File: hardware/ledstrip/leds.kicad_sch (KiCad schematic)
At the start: 4 parts, among them J5 Ledstrip connector, Q1 Q_NMOS, Q2 Q_NMOS, Q3 Q_NMOS

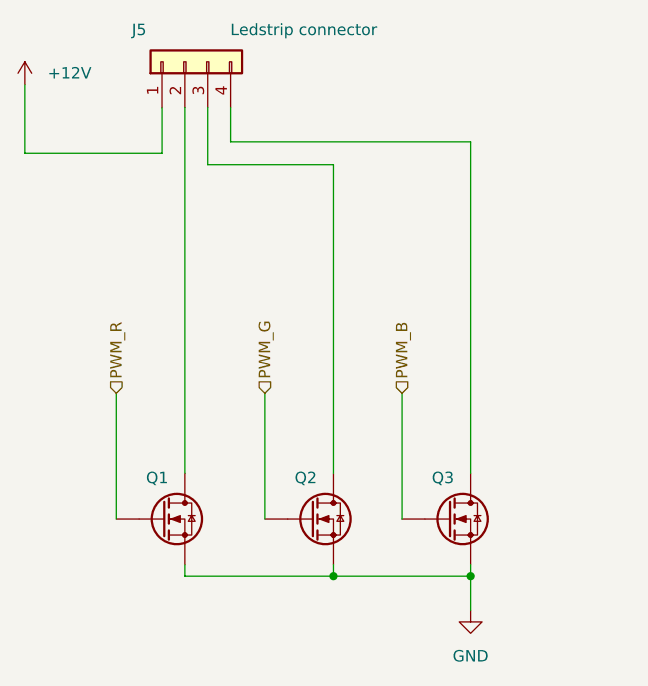
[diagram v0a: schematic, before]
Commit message: Add label on nodes.
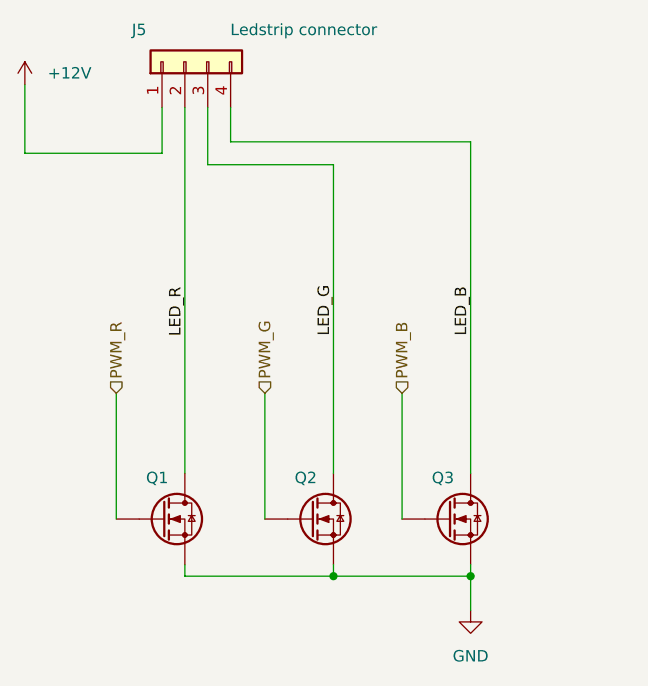
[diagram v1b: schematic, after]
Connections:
- net LED_G: now reaches J5.3 (Pin_3), Q2.D
- net LED_R: now reaches J5.2 (Pin_2), Q1.D
- net LED_B: now reaches J5.4 (Pin_4), Q3.D
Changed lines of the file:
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@@
+		)
+	)
+	(label "LED_R"
+		(at 116.84 88.9 90)
+		(effects
+			(font
+				(size 1.27 1.27)
+			)
+			(justify left bottom)
+		)
+	)
+	(label "LED_B"
+		(at 148.59 88.8363 90)
+		(effects
+			(font
+				(size 1.27 1.27)
+			)
+			(justify left bottom)
+		)
+	)
+	(label "LED_G"
+		(at 133.35 88.8363 90)
+		(effects
+			(font
+				(size 1.27 1.27)
+			)
+			(justify left bottom)
 		)
 	)

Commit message: Continue PCB.
Create netlists and color them.
Fix wrong symbol pin <-> foot print pins mapping.
Replace footprint and part for leds N-MOSFET.
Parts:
- Q1, Q2, Q3: footprint Package_TO_SOT_SMD:SOT-23_Handsoldering -> TOT-220-3:TO-220-3_Vertical; Distributor Link 1 https://www.amazon.fr/Aexit-canaux-AO3400A-Transistor-BM621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 -> https://www.mouser.fr/ProductDetail/Infineon-Technologies/I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; Distributor Link 2 https://www.digikey.fr/fr/products/detail/alpha-omega-semic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 -> https://www.digikey.fr/fr/products/detail/infineon-technolo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
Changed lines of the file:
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@@
+	(symbol
+		(lib_id "Device:Q_NMOS")
+		(at 146.05 109.22 0)
+		(unit 1)
+		(exclude_from_sim no)
+		(in_bom yes)
+		(on_board yes)
+		(dnp no)
+		(property "Reference" "Q3"
+			(at 144.272 104.648 0)
+			(effects
+				(font
+					(size 1.27 1.27)
+				)
+				(justify left)
+			)
+		)
+		(property "Value" "Q_NMOS"
+			(at 149.606 104.648 0)
+			(effects
+				(font
+					(size 1.27 1.27)
+				)
+				(justify left)
+				(hide yes)
+			)
+		)
+		(property "Footprint" "TOT-220-3:TO-220-3_Vertical"
+			(at 151.13 106.68 0)
+			(effects
+				(font
+					(size 1.27 1.27)
+				)
+				(hide yes)
+			)
+		)
+		(property "Datasheet" "https://www.mouser.fr/datasheet/3/70/1/Infineon-IRL3705N-DS-v01_02-EN.pdf"
+			(at 146.05 109.22 0)
+			(effects
+				(font
+					(size 1.27 1.27)
+				)
+				(hide yes)
+			)
+		)
+		(property "Description" "N-MOSFET transistor"
+			(at 146.05 109.22 0)
+			(effects
+				(font
+					(size 1.27 1.27)
+				)
+				(hide yes)
+			)
+		)
+		(property "Distributor Link 1" "https://www.mouser.fr/ProductDetail/Infineon-Technologies/IRL3705NPBF?qs=9%252BKlkBgLFf3RbtP30EBJKw%3D%3D"
+			(at 146.05 109.22 0)
+			(effects
+				(font
+					(size 1.27 1.27)
+				)
+				(hide yes)
+			)
+		)
+		(property "Distributor Link 2" "https://www.digikey.fr/fr/products/detail/infineon-technologies/IRL3705NPBF/812272?srsltid=AfmBOoooeDWkDS-ehnbFZ027sJbqecXx9GdmwNsCp8G_IMCaE9HrNfFl"
+			(at 146.05 109.22 0)
+			(effects
+				(font
+					(size 1.27 1.27)
+				)
+				(hide yes)
+			)
+		)
+		(pin "S"
+		)
+		(pin "D"
+		)
+		(pin "G"
+		)
+		(instances
+			(project "ledstrip"
+				(path "/dcb997ee-94c4-4df2-ba22-0e091735ddd7/ee2150f8-5f25-45fa-a64e-caf3b7331721"
+					(reference "Q3")
+					(unit 1)
+				)
+			)
+		)
+	)
+	(symbol
+		(lib_id "Device:Q_NMOS")
+		(at 114.3 109.22 0)
+		(unit 1)
+		(exclude_from_sim no)
+		(in_bom yes)
+		(on_board yes)
+		(dnp no)
+		(property "Reference" "Q1"
+			(at 112.522 104.648 0)
+			(effects
+				(font
+					(size 1.27 1.27)
+				)
+				(justify left)
+			)
+		)
+		(property "Value" "Q_NMOS"
+			(at 117.856 104.648 0)
+			(effects
+				(font
+					(size 1.27 1.27)
+				)
+				(justify left)
+				(hide yes)
+			)
+		)
+		(property "Footprint" "TOT-220-3:TO-220-3_Vertical"
+			(at 119.38 106.68 0)
+			(effects
+				(font
+					(size 1.27 1.27)
+				)
+				(hide yes)
+			)
+		)
+		(property "Datasheet" "https://www.mouser.fr/datasheet/3/70/1/Infineon-IRL3705N-DS-v01_02-EN.pdf"
+			(at 114.3 109.22 0)
+			(effects
+				(font
+					(size 1.27 1.27)
+				)
+				(hide yes)
+			)
+		)
+		(property "Description" "N-MOSFET transistor"
+			(at 114.3 109.22 0)
+			(effects
+				(font
+					(size 1.27 1.27)
+				)
+				(hide yes)
+			)
+		)
+		(property "Distributor Link 1" "https://www.mouser.fr/ProductDetail/Infineon-Technologies/IRL3705NPBF?qs=9%252BKlkBgLFf3RbtP30EBJKw%3D%3D"
+			(at 114.3 109.22 0)
+			(effects
+				(font
+					(size 1.27 1.27)
+				)
+				(hide yes)
+			)
+		)
+		(property "Distributor Link 2" "https://www.digikey.fr/fr/products/detail/infineon-technologies/IRL3705NPBF/812272?srsltid=AfmBOoooeDWkDS-ehnbFZ027sJbqecXx9GdmwNsCp8G_IMCaE9HrNfFl"
+			(at 114.3 109.22 0)
+			(effects
+				(font
+					(size 1.27 1.27)
+				)
+				(hide yes)
+			)
+		)
+		(pin "S"
+		)
+		(pin "D"
+		)
+		(pin "G"
+		)
+		(instances
+			(project ""
+				(path "/dcb997ee-94c4-4df2-ba22-0e091735ddd7/0b9dc6db-254f-4d56-b53f-9075578fa80e"
+					(reference "Q1")
+					(unit 1)
+				)
+				(path "/dcb997ee-94c4-4df2-ba22-0e091735ddd7/ee2150f8-5f25-45fa-a64e-caf3b7331721"
+					(reference "Q1")
+					(unit 1)
+				)
+			)
+		)
+	)
 	(symbol
 		(lib_id "Device:Q_NMOS")
@@
 			)
 		)
-		(property "Footprint" "Package_TO_SOT_SMD:SOT-23_Handsoldering"
+		(property "Footprint" "TOT-220-3:TO-220-3_Vertical"
 			(at 135.89 106.68 0)
 			(effects
@@
 			)
 		)
-		(property "Datasheet" "https://mm.digikey.com/Volume0/opasdata/https://mm.digikey.com/Volume0/opasdata/d220001/medias/docus/1133/AO3400A_ds.pdf/medias/docus/1133/AO3400A_ds.pdf"
+		(property "Datasheet" "https://www.mouser.fr/datasheet/3/70/1/Infineon-IRL3705N-DS-v01_02-EN.pdf"
 			(at 130.81 109.22 0)
 			(effects
@@
 			)
 		)
-		(property "Distributor Link 1" "https://www.amazon.fr/Aexit-canaux-AO3400A-Transistor-BM621825K482219I/dp/B07DD8V1JR"
+		(property "Distributor Link 1" "https://www.mouser.fr/ProductDetail/Infineon-Technologies/IRL3705NPBF?qs=9%252BKlkBgLFf3RbtP30EBJKw%3D%3D"
 			(at 130.81 109.22 0)
 			(effects
@@
 			)
 		)
-		(property "Distributor Link 2" "https://www.digikey.fr/fr/products/detail/alpha-omega-semiconductor-inc/AO3400A/1855772?srsltid=AfmBOorsNVseuGnOsg8gC49lTDXI5zjjIDAef0vv8GR8XI0_NYzzrFG-"
+		(property "Distributor Link 2" "https://www.digikey.fr/fr/products/detail/infineon-technologies/IRL3705NPBF/812272?srsltid=AfmBOoooeDWkDS-ehnbFZ027sJbqecXx9GdmwNsCp8G_IMCaE9HrNfFl"
 			(at 130.81 109.22 0)
 			(effects
@@
 				(path "/dcb997ee-94c4-4df2-ba22-0e091735ddd7/ee2150f8-5f25-45fa-a64e-caf3b7331721"
 					(reference "Q2")
-					(unit 1)
-				)
-			)
-		)
-	)
-	(symbol
-		(lib_id "Device:Q_NMOS")
-		(at 114.3 109.22 0)
-		(unit 1)
-		(exclude_from_sim no)
-		(in_bom yes)
-		(on_board yes)
-		(dnp no)
-		(property "Reference" "Q1"
-			(at 112.522 104.648 0)
-			(effects
-				(font
-					(size 1.27 1.27)
-				)
-				(justify left)
-			)
-		)
-		(property "Value" "Q_NMOS"
-			(at 117.856 104.648 0)
-			(effects
-				(font
-					(size 1.27 1.27)
-				)
-				(justify left)
-				(hide yes)
-			)
-		)
-		(property "Footprint" "Package_TO_SOT_SMD:SOT-23_Handsoldering"
-			(at 119.38 106.68 0)
-			(effects
-				(font
-					(size 1.27 1.27)
-				)
-				(hide yes)
-			)
-		)
-		(property "Datasheet" "https://mm.digikey.com/Volume0/opasdata/https://mm.digikey.com/Volume0/opasdata/d220001/medias/docus/1133/AO3400A_ds.pdf/medias/docus/1133/AO3400A_ds.pdf"
-			(at 114.3 109.22 0)
-			(effects
-				(font
-					(size 1.27 1.27)
-				)
-				(hide yes)
-			)
-		)
-		(property "Description" "N-MOSFET transistor"
-			(at 114.3 109.22 0)
-			(effects
-				(font
-					(size 1.27 1.27)
-				)
-				(hide yes)
-			)
-		)
-		(property "Distributor Link 1" "https://www.amazon.fr/Aexit-canaux-AO3400A-Transistor-BM621825K482219I/dp/B07DD8V1JR"
-			(at 114.3 109.22 0)
-			(effects
-				(font
-					(size 1.27 1.27)
-				)
-				(hide yes)
-			)
-		)
-		(property "Distributor Link 2" "https://www.digikey.fr/fr/products/detail/alpha-omega-semiconductor-inc/AO3400A/1855772?srsltid=AfmBOorsNVseuGnOsg8gC49lTDXI5zjjIDAef0vv8GR8XI0_NYzzrFG-"
-			(at 114.3 109.22 0)
-			(effects
-				(font
-					(size 1.27 1.27)
-				)
-				(hide yes)
-			)
-		)
-		(pin "S"
-		)
-		(pin "D"
-		)
-		(pin "G"
-		)
-		(instances
-			(project "ledstrip"
-				(path "/dcb997ee-94c4-4df2-ba22-0e091735ddd7/ee2150f8-5f25-45fa-a64e-caf3b7331721"
-					(reference "Q1")
 					(unit 1)
 				)
@@
 					(unit 1)
 				)
-			)
-		)
-	)
-	(symbol
-		(lib_id "Device:Q_NMOS")
-		(at 146.05 109.22 0)
-		(unit 1)
-		(exclude_from_sim no)
-		(in_bom yes)
-		(on_board yes)
-		(dnp no)
-		(property "Reference" "Q3"
-			(at 144.272 104.648 0)
-			(effects
-				(font
-					(size 1.27 1.27)
-				)
-				(justify left)
-			)
-		)
-		(property "Value" "Q_NMOS"
-			(at 149.606 104.648 0)
-			(effects
-				(font
-					(size 1.27 1.27)
-				)
-				(justify left)
-				(hide yes)
-			)
-		)
-		(property "Footprint" "Package_TO_SOT_SMD:SOT-23_Handsoldering"
-			(at 151.13 106.68 0)
-			(effects
-				(font
-					(size 1.27 1.27)
-				)
-				(hide yes)
-			)
-		)
-		(property "Datasheet" "https://mm.digikey.com/Volume0/opasdata/https://mm.digikey.com/Volume0/opasdata/d220001/medias/docus/1133/AO3400A_ds.pdf/medias/docus/1133/AO3400A_ds.pdf"
-			(at 146.05 109.22 0)
-			(effects
-				(font
-					(size 1.27 1.27)
-				)
-				(hide yes)
-			)
-		)
-		(property "Description" "N-MOSFET transistor"
-			(at 146.05 109.22 0)
-			(effects
-				(font
-					(size 1.27 1.27)
-				)
-				(hide yes)
-			)
-		)
-		(property "Distributor Link 1" "https://www.amazon.fr/Aexit-canaux-AO3400A-Transistor-BM621825K482219I/dp/B07DD8V1JR"
-			(at 146.05 109.22 0)
-			(effects
-				(font
-					(size 1.27 1.27)
-				)
-				(hide yes)
-			)
-		)
-		(property "Distributor Link 2" "https://www.digikey.fr/fr/products/detail/alpha-omega-semiconductor-inc/AO3400A/1855772?srsltid=AfmBOorsNVseuGnOsg8gC49lTDXI5zjjIDAef0vv8GR8XI0_NYzzrFG-"
-			(at 146.05 109.22 0)
-			(effects
-				(font
-					(size 1.27 1.27)
-				)
-				(hide yes)
-			)
-		)
-		(pin "S"
-		)
-		(pin "D"
-		)
-		(pin "G"
-		)
-		(instances
-			(project "ledstrip"
-				(path "/dcb997ee-94c4-4df2-ba22-0e091735ddd7/ee2150f8-5f25-45fa-a64e-caf3b7331721"
-					(reference "Q3")
-					(unit 1)
-				)

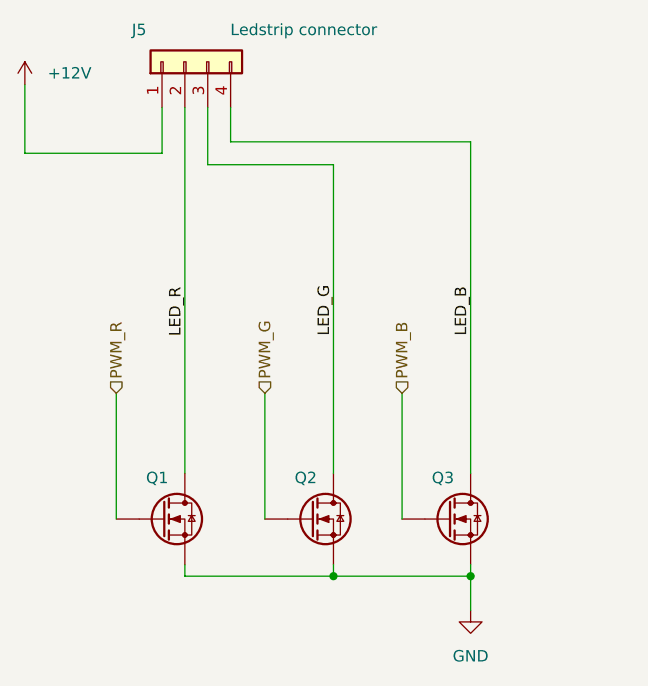
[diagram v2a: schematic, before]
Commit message: Fix ILIM_HIZ setting on BQ25703A
Add comments on schematics about hardware configuration.
Setup a early stable 2.5V from REGN to setup ILIM_HIZ correctly.
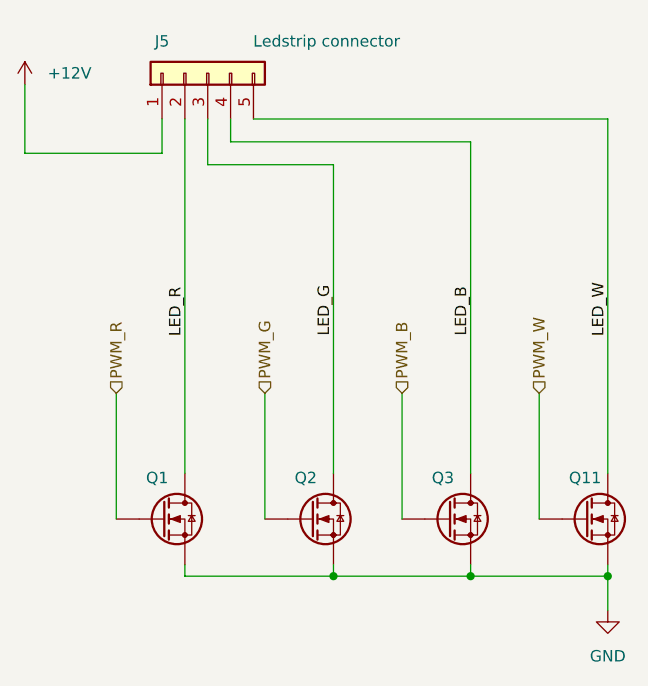
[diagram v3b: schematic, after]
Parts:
- added Q11: Q_NMOS, TOT-220-3:TO-220-3_Vertical, symbol Device:Q_NMOS
- J5: footprint Connector_JST:JST_XH_B4B-XH-A_1x04_P2.50mm_Vertical -> Connector_JST:JST_XH_B5B-XH-A_1x05_P2.50mm_Vertical; symbol Connector_Generic:Conn_01x04 -> Connector_Generic:Conn_01x05
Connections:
- net GND: now also Q11.S
- new net LED_W: J5.5 (Pin_5), Q11.D
- new net PWM_W: Q11.G
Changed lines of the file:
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@@
 		(color 0 0 0 0)
 	)
+	(junction
+		(at 163.83 115.57)
+		(diameter 0)
+		(color 0 0 0 0)
+	)
+	(wire
+		(pts
+			(xy 119.38 64.77) (xy 119.38 69.85)
+		)
+		(stroke
+			(width 0)
+			(type default)
+		)
+	)
 	(wire
 		(pts
@@
 	(wire
 		(pts
-			(xy 114.3 68.58) (xy 114.3 63.5)
-		)
-		(stroke
-			(width 0)
-			(type default)
-		)
-	)
-	(wire
-		(pts
 			(xy 148.59 114.3) (xy 148.59 115.57)
 		)
@@
 	(wire
 		(pts
+			(xy 116.84 64.77) (xy 116.84 104.14)
+		)
+		(stroke
+			(width 0)
+			(type default)
+		)
+	)
+	(wire
+		(pts
 			(xy 116.84 115.57) (xy 133.35 115.57)
 		)
@@
 	(wire
 		(pts
+			(xy 99.06 68.58) (xy 114.3 68.58)
+		)
+		(stroke
+			(width 0)
+			(type default)
+		)
+	)
+	(wire
+		(pts
+			(xy 163.83 115.57) (xy 148.59 115.57)
+		)
+		(stroke
+			(width 0)
+			(type default)
+		)
+	)
+	(wire
+		(pts
 			(xy 116.84 114.3) (xy 116.84 115.57)
 		)
@@
 	(wire
 		(pts
-			(xy 116.84 63.5) (xy 116.84 104.14)
+			(xy 109.22 95.25) (xy 109.22 109.22)
+		)
+		(stroke
+			(width 0)
+			(type default)
+		)
+	)
+	(wire
+		(pts
+			(xy 163.83 115.57) (xy 163.83 119.38)
+		)
+		(stroke
+			(width 0)
+			(type default)
+		)
+	)
+	(wire
+		(pts
+			(xy 133.35 114.3) (xy 133.35 115.57)
+		)
+		(stroke
+			(width 0)
+			(type default)
+		)
+	)
+	(wire
+		(pts
+			(xy 163.83 114.3) (xy 163.83 115.57)
+		)
+		(stroke
+			(width 0)
+			(type default)
+		)
+	)
+	(wire
+		(pts
+			(xy 156.21 95.25) (xy 156.21 109.22)
 		)
 		(stroke
@@
 	(wire
 		(pts
-			(xy 109.22 95.25) (xy 109.22 109.22)
-		)
-		(stroke
-			(width 0)
-			(type default)
-		)
-	)
-	(wire
-		(pts
-			(xy 148.59 115.57) (xy 148.59 119.38)
-		)
-		(stroke
-			(width 0)
-			(type default)
-		)
-	)
-	(wire
-		(pts
-			(xy 133.35 114.3) (xy 133.35 115.57)
-		)
-		(stroke
-			(width 0)
-			(type default)
-		)
-	)
-	(wire
-		(pts
-			(xy 121.92 63.5) (xy 121.92 67.31)
-		)
-		(stroke
-			(width 0)
-			(type default)
-		)
-	)
-	(wire
-		(pts
-			(xy 99.06 68.58) (xy 114.3 68.58)
-		)
-		(stroke
-			(width 0)
-			(type default)
-		)
-	)
-	(wire
-		(pts
-			(xy 119.38 63.5) (xy 119.38 69.85)
+			(xy 124.46 64.77) (xy 163.83 64.77)
+		)
+		(stroke
+			(width 0)
+			(type default)
+		)
+	)
+	(wire
+		(pts
+			(xy 114.3 68.58) (xy 114.3 64.77)
 		)
 		(stroke
@@
 		(pts
 			(xy 148.59 67.31) (xy 148.59 104.14)
+		)
+		(stroke
+			(width 0)
+			(type default)
+		)
+	)
+	(wire
+		(pts
+			(xy 163.83 64.77) (xy 163.83 104.14)
+		)
+		(stroke
+			(width 0)
+			(type default)
+		)
+	)
+	(wire
+		(pts
+			(xy 121.92 64.77) (xy 121.92 67.31)
 		)
 		(stroke
@@
 	(label "LED_R"
 		(at 116.84 88.9 90)
+		(effects
+			(font
+				(size 1.27 1.27)
+			)
+			(justify left bottom)
+		)
+	)
+	(label "LED_W"
+		(at 163.83 88.9 90)
 		(effects
 			(font
@@
 		(shape input)
 		(at 125.73 95.25 90)
+		(effects
+			(font
+				(size 1.27 1.27)
+			)
+			(justify left)
+		)
+	)
+	(hierarchical_label "PWM_W"
+		(shape input)
+		(at 156.21 95.25 90)
 		(effects
 			(font
@@
 	(symbol
 		(lib_id "Device:Q_NMOS")
+		(at 161.29 109.22 0)
+		(unit 1)
+		(exclude_from_sim no)
+		(in_bom yes)
+		(on_board yes)
+		(dnp no)
+		(property "Reference" "Q11"
+			(at 159.512 104.648 0)
+			(effects
+				(font
+					(size 1.27 1.27)
+				)
+				(justify left)
+			)
+		)
+		(property "Value" "Q_NMOS"
+			(at 164.846 104.648 0)
+			(effects
+				(font
+					(size 1.27 1.27)
+				)
+				(justify left)
+				(hide yes)
+			)
+		)
+		(property "Footprint" "TOT-220-3:TO-220-3_Vertical"
+			(at 166.37 106.68 0)
+			(effects
+				(font
+					(size 1.27 1.27)
+				)
+				(hide yes)
+			)
+		)
+		(property "Datasheet" "https://www.mouser.fr/datasheet/3/70/1/Infineon-IRL3705N-DS-v01_02-EN.pdf"
+			(at 161.29 109.22 0)
+			(effects
+				(font
+					(size 1.27 1.27)
+				)
+				(hide yes)
+			)
+		)
+		(property "Description" "N-MOSFET transistor"
+			(at 161.29 109.22 0)
+			(effects
+				(font
+					(size 1.27 1.27)
+				)
+				(hide yes)
+			)
+		)
+		(property "Distributor Link 1" "https://www.mouser.fr/ProductDetail/Infineon-Technologies/IRL3705NPBF?qs=9%252BKlkBgLFf3RbtP30EBJKw%3D%3D"
+			(at 161.29 109.22 0)
+			(effects
+				(font
+					(size 1.27 1.27)
+				)
+				(hide yes)
+			)
+		)
+		(property "Distributor Link 2" "https://www.digikey.fr/fr/products/detail/infineon-technologies/IRL3705NPBF/812272?srsltid=AfmBOoooeDWkDS-ehnbFZ027sJbqecXx9GdmwNsCp8G_IMCaE9HrNfFl"
+			(at 161.29 109.22 0)
+			(effects
+				(font
+					(size 1.27 1.27)
+				)
+				(hide yes)
+			)
+		)
+		(pin "S"
+		)
+		(pin "D"
+		)
+		(pin "G"
+		)
+		(instances
+			(project "ledstrip"
+				(path "/dcb997ee-94c4-4df2-ba22-0e091735ddd7/ee2150f8-5f25-45fa-a64e-caf3b7331721"
+					(reference "Q11")
+					(unit 1)
+				)
+			)
+		)
+	)
+	(symbol
+		(lib_id "Device:Q_NMOS")
 		(at 146.05 109.22 0)
 		(unit 1)
@@
 	(symbol
 		(lib_id "power:GND")
-		(at 148.59 119.38 0)
+		(at 163.83 119.38 0)
 		(unit 1)
 		(exclude_from_sim no)
@@
 		(fields_autoplaced yes)
 		(property "Reference" "#PWR017"
-			(at 148.59 125.73 0)
+			(at 163.83 125.73 0)
 			(effects
 				(font
@@
 		)
 		(property "Value" "GND"
-			(at 148.59 124.46 0)
+			(at 163.83 124.46 0)
 			(effects
 				(font
@@
 		)
 		(property "Footprint" ""
-			(at 148.59 119.38 0)
+			(at 163.83 119.38 0)
 			(effects
 				(font
@@
 		)
 		(property "Datasheet" ""
-			(at 148.59 119.38 0)
+			(at 163.83 119.38 0)
 			(effects
 				(font
@@
 		)
 		(property "Description" "Power symbol creates a global label with name \"GND\" , ground"
-			(at 148.59 119.38 0)
+			(at 163.83 119.38 0)
 			(effects
 				(font
@@
 	)
 	(symbol
-		(lib_id "Connector_Generic:Conn_01x04")
-		(at 116.84 58.42 90)
+		(lib_id "Connector_Generic:Conn_01x05")
+		(at 119.38 59.69 90)
 		(unit 1)
 		(exclude_from_sim no)
@@
 		(dnp no)
 		(property "Reference" "J5"
-			(at 111.76 54.864 90)
+			(at 114.3 56.134 90)
 			(effects
 				(font
@@
 		)
 		(property "Value" "Ledstrip connector"
-			(at 130.048 54.864 90)
-			(effects
-				(font
-					(size 1.27 1.27)
-				)
-			)
-		)
-		(property "Footprint" "Connector_JST:JST_XH_B4B-XH-A_1x04_P2.50mm_Vertical"
-			(at 116.84 58.42 0)
+			(at 132.588 56.134 90)
+			(effects
+				(font
+					(size 1.27 1.27)
+				)
+			)
+		)
+		(property "Footprint" "Connector_JST:JST_XH_B5B-XH-A_1x05_P2.50mm_Vertical"
+			(at 119.38 59.69 0)
 			(effects
 				(font
@@
 		)
 		(property "Datasheet" "~"
-			(at 116.84 58.42 0)
-			(effects
-				(font
-					(size 1.27 1.27)
-				)
-				(hide yes)
-			)
-		)
-		(property "Description" "Generic connector, single row, 01x04, script generated (kicad-library-utils/schlib/autogen/connector/)"
-			(at 116.84 58.42 0)
+			(at 119.38 59.69 0)
+			(effects
+				(font
+					(size 1.27 1.27)
+				)
+				(hide yes)
+			)
+		)
+		(property "Description" "Generic connector, single row, 01x05, script generated (kicad-library-utils/schlib/autogen/connector/)"
+			(at 119.38 59.69 0)
 			(effects
 				(font
@@
 		(pin "2"
 		)
+		(pin "5"
+		)
 		(instances

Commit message: Fix ERC and DRC errors.
Use a custom copy of USB-C in project library to avoid having a version
mismatch with CI.
Fix QFN-20-1EP_3x4mm_P0.5mm_EP1.65x2.65mm_ThermalVias  mismatch pins.
Fix ERC errors.
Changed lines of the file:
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@@
 	(paper "A4")
+	(junction
+		(at 106.68 68.58)
+		(diameter 0)
+		(color 0 0 0 0)
+	)
 	(junction
 		(at 133.35 115.57)
@@
 	(wire
 		(pts
-			(xy 99.06 68.58) (xy 114.3 68.58)
+			(xy 99.06 68.58) (xy 106.68 68.58)
 		)
 		(stroke
@@
 		(pts
 			(xy 148.59 67.31) (xy 148.59 104.14)
+		)
+		(stroke
+			(width 0)
+			(type default)
+		)
+	)
+	(wire
+		(pts
+			(xy 106.68 68.58) (xy 114.3 68.58)
 		)
 		(stroke
@@
 					(unit 1)
 				)
+			)
+		)
+	)
+	(symbol
+		(lib_id "power:PWR_FLAG")
+		(at 106.68 68.58 0)
+		(unit 1)
+		(exclude_from_sim no)
+		(in_bom yes)
+		(on_board yes)
+		(dnp no)
+		(fields_autoplaced yes)
+		(property "Reference" "#FLG09"
+			(at 106.68 66.675 0)
+			(effects
+				(font
+					(size 1.27 1.27)
+				)
+				(hide yes)
+			)
+		)
+		(property "Value" "PWR_FLAG"
+			(at 106.68 63.5 0)
+			(effects
+				(font
+					(size 1.27 1.27)
+				)
+			)
+		)
+		(property "Footprint" ""
+			(at 106.68 68.58 0)
+			(effects
+				(font
+					(size 1.27 1.27)
+				)
+				(hide yes)
+			)
+		)
+		(property "Datasheet" "~"
+			(at 106.68 68.58 0)
+			(effects
+				(font
+					(size 1.27 1.27)
+				)
+				(hide yes)
+			)
+		)
+		(property "Description" "Special symbol for telling ERC where power comes from"
+			(at 106.68 68.58 0)
+			(effects
+				(font
+					(size 1.27 1.27)
+				)
+				(hide yes)
+			)
+		)
+		(pin "1"
+		)
+		(instances
+			(project ""
+				(path "/dcb997ee-94c4-4df2-ba22-0e091735ddd7/ee2150f8-5f25-45fa-a64e-caf3b7331721"
+					(reference "#FLG09")
+					(unit 1)
+				)
